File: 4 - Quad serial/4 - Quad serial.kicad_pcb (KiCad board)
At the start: 2 copper layers, 100 x 100 mm, 59 parts, among them J1 EDGE, J2 INT READ, J3 SIO CLK SRC, J4 COM1: DCE, J5 COM2: DTE, J6 SIO CLK SRC, J7 COM3: USB B, J8 COM4: USB A, U1 74HCT32, U10 MCP2221A, U11 MCP2221A, U12 Z84C3010, U2 74HCT148, U3 74HCT573, U4 74HCT563, U5 74HCT138, U6 Z84C4010, U7 MAX232, U8 MAX232, U9 Z84C4010, X1 3.6864 MHz

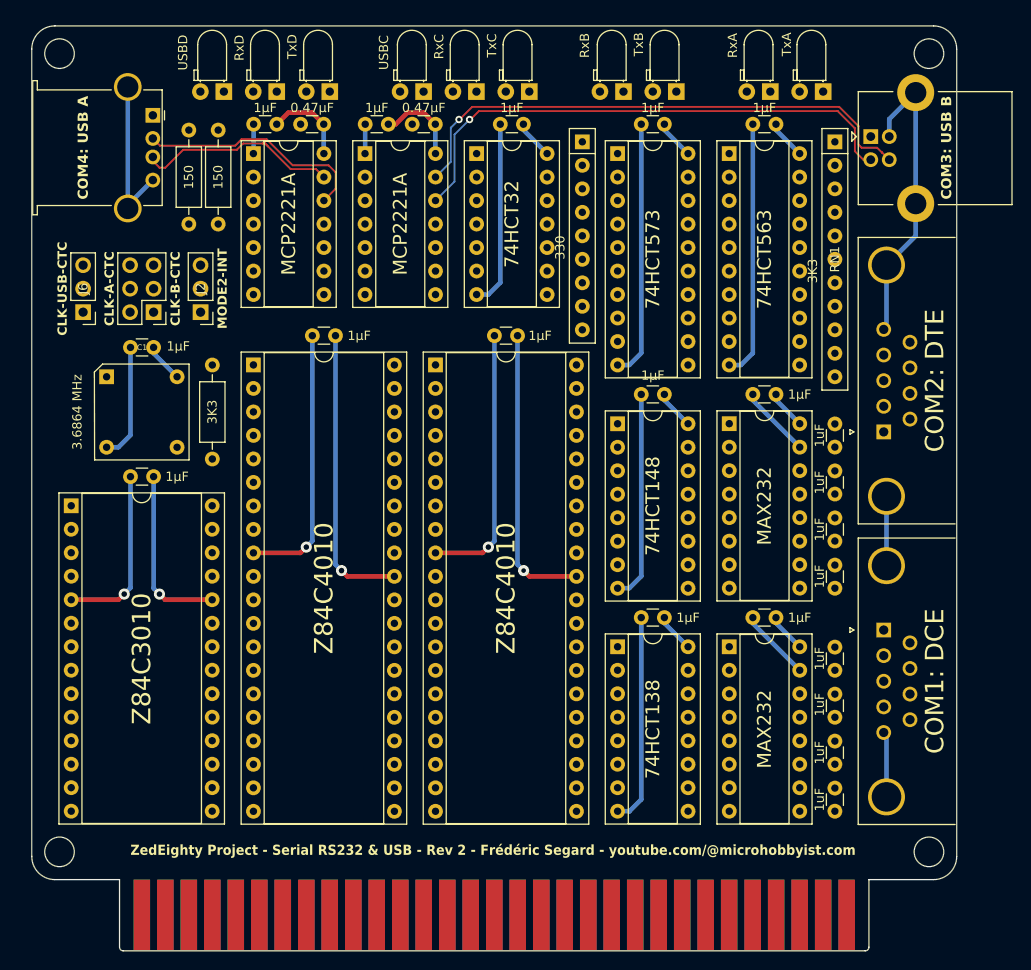
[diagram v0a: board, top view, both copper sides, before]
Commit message: Made a mess of things a bit.
Software clock is non-functional. Worked on the breadboard, but makes the CPU board crash when writing to the IO port to select clock speed.
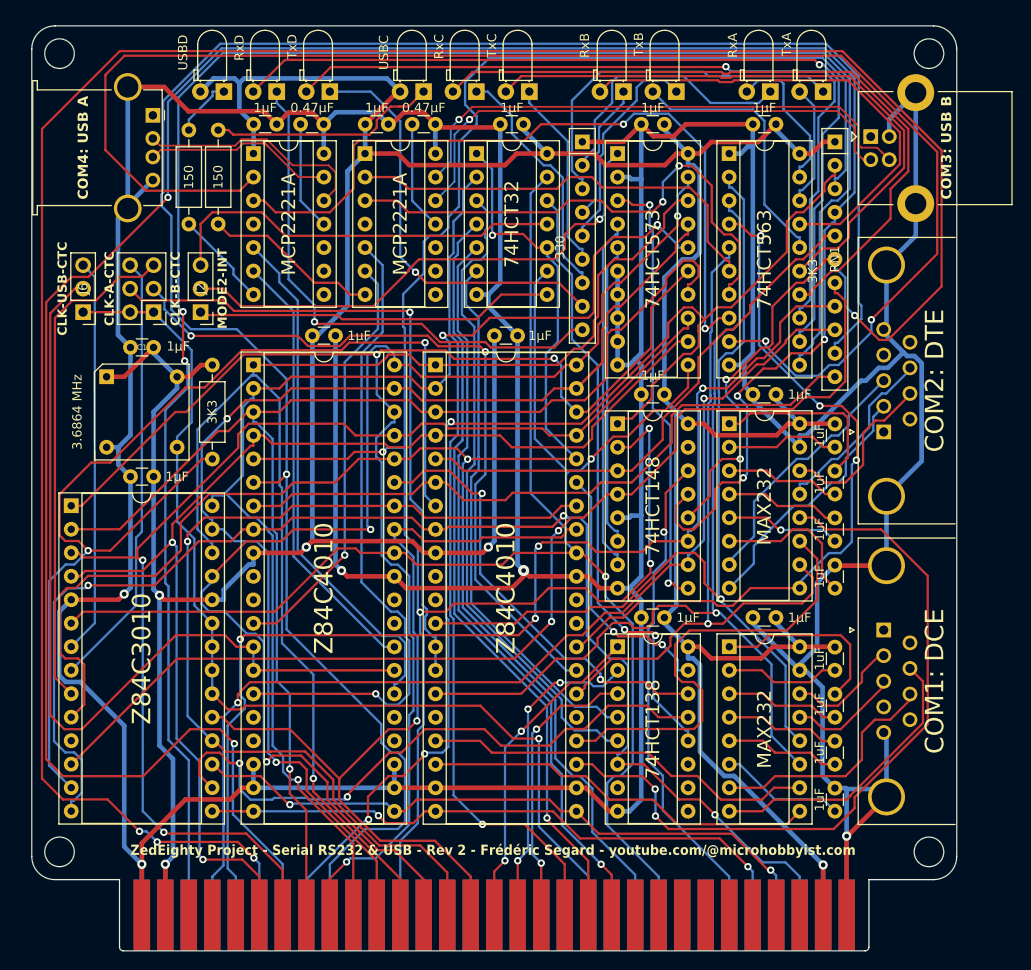
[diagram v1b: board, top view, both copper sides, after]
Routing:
- net GND: track 315.4 -> 658.2 mm, vias 3 -> 5
- net +5V: track 117.3 -> 438.8 mm, vias 3 -> 5
- net /~{IRQ}5: track 0.00 -> 281.7 mm, vias 0 -> 6
- net /~{IRQ}4: track 0.00 -> 266.1 mm, vias 0 -> 5
- net /IE: track 0.00 -> 222.4 mm, vias 0 -> 1
- net /~{IRQ}2: track 0.00 -> 216.7 mm, vias 0 -> 4
- net /~{CLK}: track 0.00 -> 200.3 mm, vias 0 -> 2
- net /~{M1}: track 0.00 -> 193.8 mm, vias 0 -> 4
- net /~{IORQ}: track 0.00 -> 179.4 mm, vias 0 -> 2
- net /RxD: track 0.00 -> 163.3 mm, vias 0 -> 2
- net /D4: track 0.00 -> 157.1 mm, vias 0 -> 3
- net /~{RD}: track 0.00 -> 148.5 mm, vias 0 -> 1
- net /D1: track 0.00 -> 148.5 mm, vias 0 -> 1
- net /D0: track 0.00 -> 145.2 mm, vias 0 -> 3
- net /D5: track 0.00 -> 144.9 mm, vias 0 -> 1
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
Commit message: Rerouted some traces and readied the the gerber to send out to manufacturing
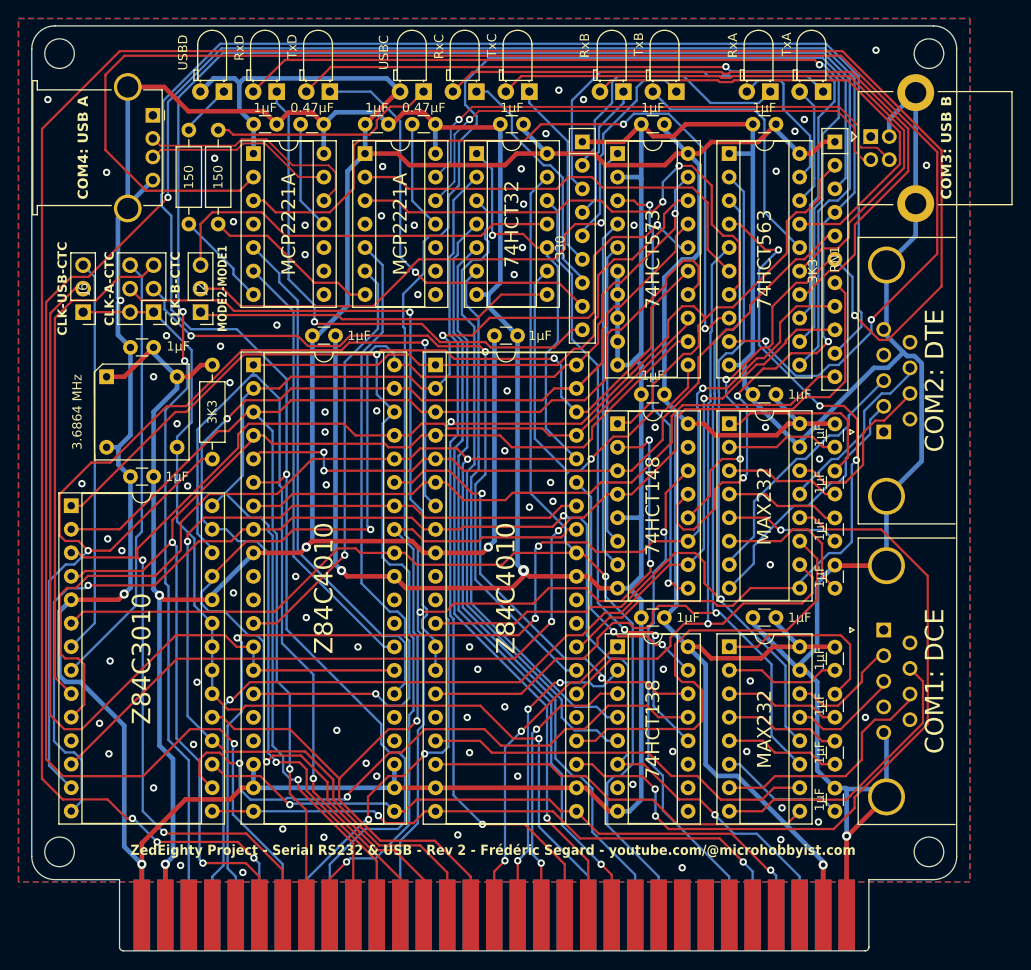
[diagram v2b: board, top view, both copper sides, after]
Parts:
- C10, C11, C12, C13, C14, C15, C16, C17: value 1uF -> 1µF
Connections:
- U9 pad 5: /~{IRQ}2 -> /~{IRQ}1
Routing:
- net /~{IRQ}1: track 57.8 -> 80.1 mm, vias 0 -> 2
- net /~{IRQ}2: track 216.7 -> 198.0 mm, vias 4 -> 3
- net /D0: track 145.2 -> 142.4 mm
- net /RxB: track 78.4 -> 80.4 mm
- net /D2: track 135.8 -> 134.2 mm
- net /COM 3 and 4 (USB)/D1+: track 59.4 -> 57.9 mm
- net Net-(D2-K): track 30.8 -> 29.4 mm
- net Net-(D9-K): track 25.9 -> 24.8 mm
- net +5V: track 438.8 -> 437.8 mm
- net Net-(D1-K): track 40.2 -> 39.3 mm
- net GND: track 658.2 -> 657.3 mm, vias 5 -> 86
- net /COM 3 and 4 (USB)/D2+: track 21.4 -> 20.6 mm
- net Net-(D10-K): track 6.45 -> 5.73 mm
- net /D3: track 131.2 -> 130.5 mm
- net /~{IRQ}4: track 266.1 -> 266.8 mm
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- added copper zone on B.Cu, net GND
- added copper zone on F.Cu, net GND
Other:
- board text added: "MODE2-MODE1"
- board text removed: "MODE2-INT"
